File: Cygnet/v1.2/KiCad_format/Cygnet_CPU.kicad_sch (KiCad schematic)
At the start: 38 parts, among them J4 BM04B-SRSS-TBT(LF)(SN), J5 FTSH-107-01-L-DV-K, SW1 PB-SKRPADE010, SW2 PB-SKRPABE010, SW3 PB-SKRPADE010, U1 STM32L433, Y1 ABS06-107-32.768KHZ-T

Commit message: Ports: fill in the MPNs the old BOM gate was hiding
With the BOM comparator no longer treating a blank KiCad MPN as agreement, four
boards turned out to be missing manufacturer part numbers that their shipped
BOMs specify. None of this was visible before, because the comparison skipped
any refdes whose KiCad MPN was empty and then reported "BOM matches exactly".

  Cygnet          74 parts, none of which carried an MPN field at all
  Scoop           C3, U2, U4
  Notecarrier-XI  J9
  Mojo            R2, R3 - the only two parts on the board lacking the
                  MANUFACTURER PART NUMBER field their peers all carry

Filled from each board's own shipped BOM, which is authoritative for what was
built, using the field name that board's config already declares. There was no
conflict to resolve: the KiCad side held nothing.

Verified: all eight boards with a BOM gate now pass, every edited schematic
exports an identical netlist before and after, and kicanvas renders all of them.
Mojo's full battery is green end to end (ERC, DRC, BOM, gerber diff, placement,
kicanvas, RAG), with NETLIST skipped under its declared justification.

Co-Authored-By: Claude Fable 5 <noreply@anthropic.com>
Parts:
- C1: MPN (none) -> c1608x5r1a475k/0.50
- C10, C6: MPN (none) -> c0402b105k016t
- C11, C7: MPN (none) -> grm033r61c103ka12d
- C12, C13: MPN (none) -> grm0335c1h4r0ba01d
- C14, C15, C16, C2, C3, C4, C5, C8, C9: MPN (none) -> grm033r61c104ke84j
- J4: MPN (none) -> bm04b-srss-tbt(lf)(sn)
- J5: MPN (none) -> ftsh-107-01-l-dv-k
- LD1: MPN (none) -> sml-p12u2tt86r
- R1, R10, R2, R5, R6, R8, R9: MPN (none) -> mc0201l6f1002se
- R3: MPN (none) -> rk73h1httc1005f
- R4: MPN (none) -> rk73h1httc4304f
- R7: MPN (none) -> crcw02011k00fned
- SW1, SW3: MPN (none) -> skrpade010
- SW2: MPN (none) -> skrpabe010
- TVS1, TVS2, TVS3: MPN (none) -> esd5z3.3t1g
- U1: MPN (none) -> stm32l433cb
- Y1: MPN (none) -> abs06-107-32.768khz-t

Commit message: Ports: restore shipped-BOM letter case in the backfilled MPN fields
The 78-MPN backfill (d1a1499) said "filled from each board's own shipped BOM"
but inserted the comparison's casefolded text, not the spreadsheets' - every
shipped BOM involved is uppercase (SKRPADE010, CC0603KRX7R7BB105,
TSW-105-07-F-D), and the gate only agreed because its comparison is
case-insensitive. The lowercase text was user-visible in the schematic fields
and flowed into the RAG extract's new MPN column.

Restored the spreadsheets' exact text on all 78 fields (Cygnet 74, Scoop 3,
XI 1; Mojo's two were inserted correctly), scoped to exactly the property
values that commit added. Verified inert: the BOM gate passes on all three
boards and the re-exported netlists differ only in the affected field text.

Co-Authored-By: Claude Fable 5 <noreply@anthropic.com>
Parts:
- C1: MPN c1608x5r1a475k/0.50 -> C1608X5R1A475K/0.50
- C10, C6: MPN c0402b105k016t -> C0402B105K016T
- C11, C7: MPN grm033r61c103ka12d -> GRM033R61C103KA12D
- C12, C13: MPN grm0335c1h4r0ba01d -> GRM0335C1H4R0BA01D
- C14, C15, C16, C2, C3, C4, C5, C8, C9: MPN grm033r61c104ke84j -> GRM033R61C104KE84J
- J4: MPN bm04b-srss-tbt(lf)(sn) -> BM04B-SRSS-TBT(LF)(SN)
- J5: MPN ftsh-107-01-l-dv-k -> FTSH-107-01-L-DV-K
- LD1: MPN sml-p12u2tt86r -> SML-P12U2TT86R
- R1, R10, R2, R5, R6, R8, R9: MPN mc0201l6f1002se -> MC0201L6F1002SE
- R3: MPN rk73h1httc1005f -> RK73H1HTTC1005F
- R4: MPN rk73h1httc4304f -> RK73H1HTTC4304F
- R7: MPN crcw02011k00fned -> CRCW02011K00FNED
- SW1, SW3: MPN skrpade010 -> SKRPADE010
- SW2: MPN skrpabe010 -> SKRPABE010
- TVS1, TVS2, TVS3: MPN esd5z3.3t1g -> ESD5Z3.3T1G
- U1: MPN stm32l433cb -> STM32L433CB
- Y1: MPN abs06-107-32.768khz-t -> ABS06-107-32.768KHZ-T
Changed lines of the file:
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@@
 				(justify right bottom)
 			)
-		)		(property "MPN" "skrpabe010"
+		)		(property "MPN" "SKRPABE010"
 			(at 275.2 236.9622 0)
 			(effects
@@
 				(justify left bottom)
 			)
-		)		(property "MPN" "c0402b105k016t"
+		)		(property "MPN" "C0402B105K016T"
 			(at 72.5 62.0022 0)
 			(effects
@@
 				(justify right bottom)
 			)
-		)		(property "MPN" "mc0201l6f1002se"
+		)		(property "MPN" "MC0201L6F1002SE"
 			(at 319.96 49.4622 0)
 			(effects
@@
 				(justify right bottom)
 			)
-		)		(property "MPN" "sml-p12u2tt86r"
+		)		(property "MPN" "SML-P12U2TT86R"
 			(at 150 239.5022 0)
 			(effects
@@
 				(justify left bottom)
 			)
-		)		(property "MPN" "grm033r61c104ke84j"
+		)		(property "MPN" "GRM033R61C104KE84J"
 			(at 47.5 62.1222 0)
 			(effects
@@
 				(justify right bottom)
 			)
-		)		(property "MPN" "c1608x5r1a475k/0.50"
+		)		(property "MPN" "C1608X5R1A475K/0.50"
 			(at 42.5 64.5022 0)
 			(effects
@@
 				(justify left bottom)
 			)
-		)		(property "MPN" "c0402b105k016t"
+		)		(property "MPN" "C0402B105K016T"
 			(at 95 62.9382 0)
 			(effects
@@
 				(justify right bottom)
 			)
-		)		(property "MPN" "mc0201l6f1002se"
+		)		(property "MPN" "MC0201L6F1002SE"
 			(at 239.96 209.4622 0)
 			(effects
@@
 				(justify right bottom)
 			)
-		)		(property "MPN" "rk73h1httc4304f"
+		)		(property "MPN" "RK73H1HTTC4304F"
 			(at 149.96 119.4622 0)
 			(effects
@@
 				(justify right bottom)
 			)
-		)		(property "MPN" "mc0201l6f1002se"
+		)		(property "MPN" "MC0201L6F1002SE"
 			(at 77.46 221.9622 0)
 			(effects
@@
 				(justify right bottom)
 			)
-		)		(property "MPN" "skrpade010"
+		)		(property "MPN" "SKRPADE010"
 			(at 274.8 272.1622 0)
 			(effects
@@
 				(justify left bottom)
 			)
-		)		(property "MPN" "skrpade010"
+		)		(property "MPN" "SKRPADE010"
 			(at 276 195.5022 0)
 			(effects
@@
 				(justify left bottom)
 			)
-		)		(property "MPN" "grm0335c1h4r0ba01d"
+		)		(property "MPN" "GRM0335C1H4R0BA01D"
 			(at 325 147.0022 0)
 			(effects
@@
 				(justify right bottom)
 			)
-		)		(property "MPN" "grm033r61c104ke84j"
+		)		(property "MPN" "GRM033R61C104KE84J"
 			(at 277.5 272.0022 0)
 			(effects
@@
 				(justify left bottom)
 			)
-		)		(property "MPN" "grm033r61c104ke84j"
+		)		(property "MPN" "GRM033R61C104KE84J"
 			(at 52.5 62.1222 0)
 			(effects
@@
 				(justify right bottom)
 			)
-		)		(property "MPN" "esd5z3.3t1g"
+		)		(property "MPN" "ESD5Z3.3T1G"
 			(at 273.18 216.9622 0)
 			(effects
@@
 				(hide yes)
 			)
-		)		(property "MPN" "abs06-107-32.768khz-t"
+		)		(property "MPN" "ABS06-107-32.768KHZ-T"
 			(at 329.88 132.0022 0)
 			(effects
@@
 				(justify right bottom)
 			)
-		)		(property "MPN" "grm033r61c104ke84j"
+		)		(property "MPN" "GRM033R61C104KE84J"
 			(at 277.5 244.5022 0)
 			(effects
@@
 				(justify left bottom)
 			)
-		)		(property "MPN" "grm033r61c104ke84j"
+		)		(property "MPN" "GRM033R61C104KE84J"
 			(at 90 62.1222 0)
 			(effects
@@
 				(justify right bottom)
 			)
-		)		(property "MPN" "esd5z3.3t1g"
+		)		(property "MPN" "ESD5Z3.3T1G"
 			(at 274.88 276.9622 0)
 			(effects
@@
 				(justify right bottom)
 			)
-		)		(property "MPN" "rk73h1httc1005f"
+		)		(property "MPN" "RK73H1HTTC1005F"
 			(at 149.96 102.1222 0)
 			(effects
@@
 				(justify left bottom)
 			)
-		)		(property "MPN" "grm0335c1h4r0ba01d"
+		)		(property "MPN" "GRM0335C1H4R0BA01D"
 			(at 342.5 146.0662 0)
 			(effects
@@
 				(justify right bottom)
 			)
-		)		(property "MPN" "ftsh-107-01-l-dv-k"
+		)		(property "MPN" "FTSH-107-01-L-DV-K"
 			(at 72.5 224.5022 0)
 			(effects
@@
 				(justify right bottom)
 			)
-		)		(property "MPN" "mc0201l6f1002se"
+		)		(property "MPN" "MC0201L6F1002SE"
 			(at 212.46 221.9622 0)
 			(effects
@@
 				(justify right bottom)
 			)
-		)		(property "MPN" "bm04b-srss-tbt(lf)(sn)"
+		)		(property "MPN" "BM04B-SRSS-TBT(LF)(SN)"
 			(at 360 222.0022 0)
 			(effects
@@
 				(justify left bottom)
 			)
-		)		(property "MPN" "grm033r61c104ke84j"
+		)		(property "MPN" "GRM033R61C104KE84J"
 			(at 57.5 62.1222 0)
 			(effects
@@
 				(justify right bottom)
 			)
-		)		(property "MPN" "grm033r61c104ke84j"
+		)		(property "MPN" "GRM033R61C104KE84J"
 			(at 275.8 212.0022 0)
 			(effects
@@
 				(justify left bottom)
 			)
-		)		(property "MPN" "grm033r61c104ke84j"
+		)		(property "MPN" "GRM033R61C104KE84J"
 			(at 67.5 62.1222 0)
 			(effects
@@
 				(justify right bottom)
 			)
-		)		(property "MPN" "crcw02011k00fned"
+		)		(property "MPN" "CRCW02011K00FNED"
 			(at 147.46 222.1222 0)
 			(effects
@@
 				(justify right bottom)
 			)
-		)		(property "MPN" "stm32l433cb"
+		)		(property "MPN" "STM32L433CB"
 			(at 220 62.0022 0)
 			(effects
@@
 				(justify left bottom)
 			)
-		)		(property "MPN" "grm033r61c103ka12d"
+		)		(property "MPN" "GRM033R61C103KA12D"
 			(at 160 117.0022 0)
 			(effects
@@
 				(justify right bottom)
 			)
-		)		(property "MPN" "mc0201l6f1002se"
+		)		(property "MPN" "MC0201L6F1002SE"
 			(at 204.96 221.9622 0)
 			(effects
@@
 				(justify right bottom)
 			)
-		)		(property "MPN" "mc0201l6f1002se"
+		)		(property "MPN" "MC0201L6F1002SE"
 			(at 324.96 49.6222 0)
 			(effects
@@
 				(justify left bottom)
 			)
-		)		(property "MPN" "grm033r61c103ka12d"
+		)		(property "MPN" "GRM033R61C103KA12D"
 			(at 77.5 60.4382 0)
 			(effects
@@
 				(justify left bottom)
 			)
-		)		(property "MPN" "grm033r61c104ke84j"
+		)		(property "MPN" "GRM033R61C104KE84J"
 			(at 112.5 62.0022 0)
 			(effects
@@
 				(justify right bottom)
 			)
-		)		(property "MPN" "mc0201l6f1002se"
+		)		(property "MPN" "MC0201L6F1002SE"
 			(at 77.46 244.4622 0)
 			(effects
@@
 				(justify right bottom)
 			)
-		)		(property "MPN" "esd5z3.3t1g"
+		)		(property "MPN" "ESD5Z3.3T1G"
 			(at 274.88 249.4622 0)
 			(effects

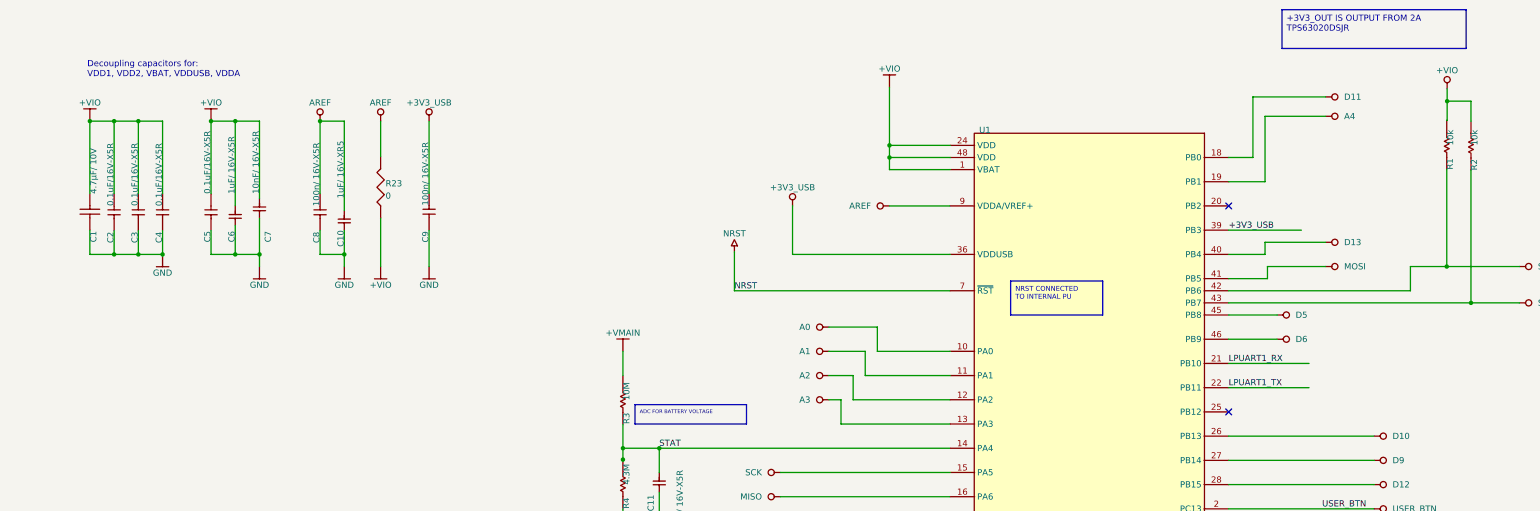
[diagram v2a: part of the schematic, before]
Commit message: Ports: convert design-note text_boxes to plain text so kicanvas can render them
kicanvas parses text_box but never paints it - true of the current upstream
build too, which is byte-identical to the one vendored here. On the published
datasheet pages that left the design notes (charger limits, regulator specs,
population notes) as empty frames, and on Cygnet, whose note frames ARE the
text_boxes, the notes were entirely invisible. KiCad renders plain text and
rectangles identically to what it drew before, and kicanvas renders both, so
the 28 text_boxes across 12 sheets on 6 boards become plain text items - plus a
synthesized rectangle carrying the exact stroke and fill for the 5 Cygnet notes
whose box itself is visible (yellow-filled with a border).

Two things made this more than a mechanical swap:

- text_box soft-wraps and plain text does not. A first attempt left two notes
  overflowing their frames and colliding with a neighbouring note. The wrap is
  now frozen at exactly the line breaks KiCad itself used: each sheet's
  before-conversion PDF carries a hidden searchable text layer, and the
  converter reads the wrapped lines out of the note's own rectangle, guarded by
  a word-for-word equality check against the source text. That guard earned its
  keep twice, catching part-number labels that physically overlap two of the
  note boxes.

- kicanvas draws default-colored text in its theme color, which is white - and
  two Cygnet notes sit on yellow fills. Those five framed notes now carry an
  explicit (0,0,193) font color, sampled from KiCad's own plot of the same
  notes, so KiCad's output is unchanged and kicanvas is readable.

Verified per board: netlists byte-equal before and after; KiCad PDF renders
differ only by sub-millimetre line pitch (0.05-0.7% of sampled pixels, every
note inside its frame - checked visually on the worst sheets); kicanvas renders
all 12 sheets with the notes now visible; committed screenshots regenerated,
all six boards PASS.

Co-Aut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
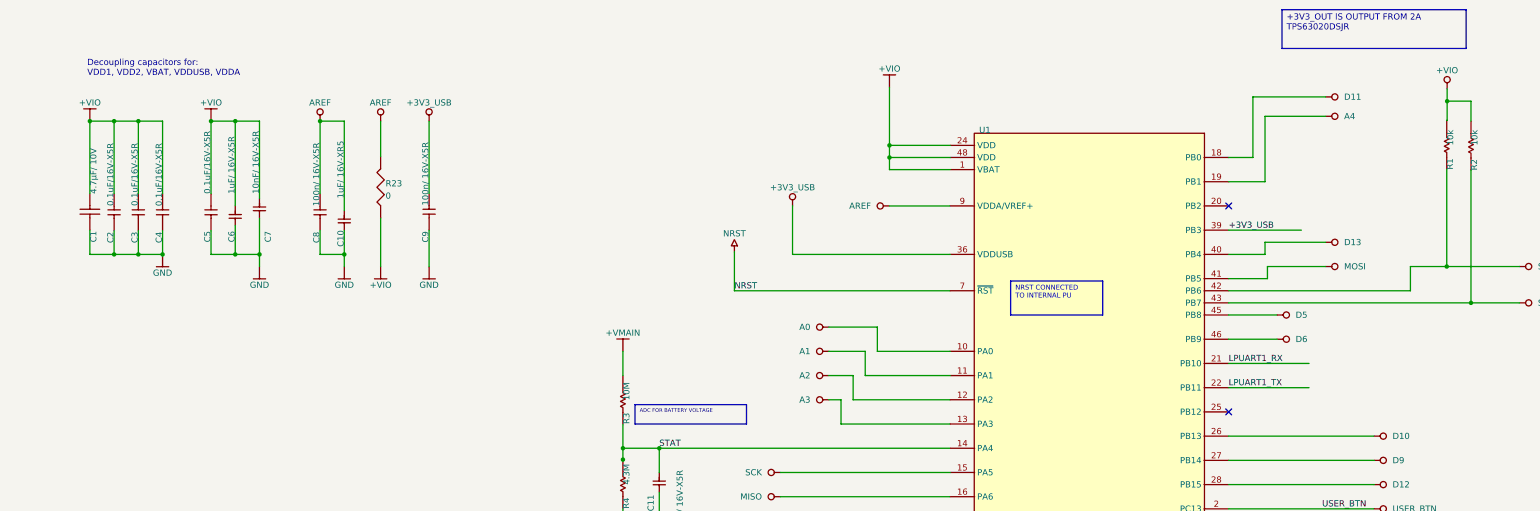
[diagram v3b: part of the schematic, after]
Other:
- note added: "+3V3_OUT IS OUTPUT FROM 2A TPS63020DSJR"
- note added: "ADC FOR BATTERY VOLTAGE"
- note added: "Decoupling capacitors for: VDD1, VDD2, VBAT, VDDUSB, VDDA"
- note added: "NRST CONNECTED TO INTERNAL PU"
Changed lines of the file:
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@@
 		)
 	)
-	(text_box "ADC FOR BATTERY VOLTAGE"
-		(exclude_from_sim no)
-		(at 178 100.5022 0)
-		(size -23 4)
-		(margins 0.9525 0.9525 0.9525 0.9525)
+	(rectangle
+		(start 155 100.502)
+		(end 178 104.502)
 		(stroke
 			(width 0)
@@
 			(color 255 255 150 1)
 		)
+	)
+	(text "ADC FOR BATTERY VOLTAGE"
+		(exclude_from_sim no)
+		(at 155.952 101.455 0)
 		(effects
 			(font
 				(size 0.762 0.762)
+				(color 0 0 193 1)
 			)
 			(justify left top)
 		)
 	)
-	(text_box "Decoupling capacitors for:\nVDD1, VDD2, VBAT, VDDUSB, VDDA"
+	(text "Decoupling capacitors for:\nVDD1, VDD2, VBAT, VDDUSB, VDDA"
 		(exclude_from_sim no)
-		(at 81.98 28.3822 0)
-		(size -40.98 7.62)
-		(margins 0.9525 0.9525 0.9525 0.9525)
-		(stroke
-			(width -0.0001)
-			(type default)
-			(color 0 0 0 1)
-		)
-		(fill
-			(type none)
-		)
+		(at 41.9525 29.3347 0)
 		(effects
 			(font
@@
 		)
 	)
-	(text_box "+3V3_OUT IS OUTPUT FROM 2A TPS63020DSJR"
-		(exclude_from_sim no)
-		(at 326.5 19.0022 0)
-		(size -38 8)
-		(margins 0.9525 0.9525 0.9525 0.9525)
+	(rectangle
+		(start 288.5 19.0022)
+		(end 326.5 27.0022)
 		(stroke
 			(width 0)
@@
 			(color 255 255 150 1)
 		)
+	)
+	(text "+3V3_OUT IS OUTPUT FROM 2A\nTPS63020DSJR"
+		(exclude_from_sim no)
+		(at 289.452 19.9547 0)
 		(effects
 			(font
 				(size 1.27 1.27)
+				(color 0 0 193 1)
 			)
 			(justify left top)
 		)
 	)
-	(text_box "NRST CONNECTED \nTO INTERNAL PU"
-		(exclude_from_sim no)
-		(at 251.5 75.0022 0)
-		(size -19 7)
-		(margins 0.9525 0.9525 0.9525 0.9525)
+	(rectangle
+		(start 232.5 75.0022)
+		(end 251.5 82.0022)
 		(stroke
 			(width 0)
@@
 			(color 255 255 150 1)
 		)
+	)
+	(text "NRST CONNECTED\nTO INTERNAL PU"
+		(exclude_from_sim no)
+		(at 233.452 75.9547 0)
 		(effects
 			(font
 				(size 1.016 1.016)
+				(color 0 0 193 1)
 			)
 			(justify left top)
